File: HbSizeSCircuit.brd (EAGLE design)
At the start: 38.8 x 45.9 mm, 20 parts

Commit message: add left board file
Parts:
- moved R1 88.1 mm to (-47.0, 44.5), turned to 0 degrees
- moved 100KΩ 87.6 mm to (-48.3, 49.5), flipped to the top, turned to 0 degrees
- moved U$12 80.3 mm to (-38.1, 52.1), flipped to the top, turned to 0 degrees
- moved R2 76.8 mm to (-49.5, 31.8)
- moved U$5 72.9 mm to (-35.6, 55.9)
- moved C1 66.5 mm to (-35.6, 44.5), turned to 0 degrees
- moved R3 65.9 mm to (-16.5, 44.5), turned to 0 degrees
- moved C2 65.5 mm to (-41.9, 44.5)
- moved U$2 64.0 mm to (-41.9, 33.0)
- moved U$8 61.3 mm to (-45.7, 1.27)
- moved U$11 60.9 mm to (-27.9, 52.1), flipped to the top
- moved R5 58.3 mm to (-29.2, 44.5), turned to 0 degrees
- moved U$4 58.1 mm to (-29.2, 55.9)
- moved U$9 50.4 mm to (-17.8, 52.1), flipped to the top
- moved U$6 50.3 mm to (-22.9, 14.0), flipped to the top, turned to 0 degrees
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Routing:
- net GND: track 142.9 -> 0.00 mm, vias 5 -> 0
- net +5V: track 72.8 -> 0.00 mm, vias 4 -> 0
- net V+: track 48.4 -> 0.00 mm
- net PIN_THUMBSERVO: track 38.0 -> 0.00 mm
- net SWITCH_INIT: track 36.3 -> 0.00 mm, vias 1 -> 0
- net PIN_ON/OFF: track 32.0 -> 0.00 mm, vias 1 -> 0
- net SWITCH_THUMB: track 30.8 -> 0.00 mm, vias 1 -> 0
- net PIN_INDEXSERVO: track 30.0 -> 0.00 mm
- net PGOOD: track 30.0 -> 0.00 mm, vias 1 -> 0
- net PIN_OTHERSERVO: track 26.4 -> 0.00 mm, vias 2 -> 0
- net SENSOR: track 25.3 -> 0.00 mm, vias 1 -> 0
- net SWITCH_MODE: track 23.8 -> 0.00 mm, vias 1 -> 0
- net SWITCH_HOLD: track 9.90 -> 0.00 mm, vias 1 -> 0
- net N$1: track 3.46 -> 0.00 mm
- net N$2: track 2.66 -> 0.00 mm
- removed copper zone on layer 1, net GND
- removed copper zone on layer 16, net GND
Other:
- board size 38.8 x 45.9 mm -> 6.1 x 10.3 mm

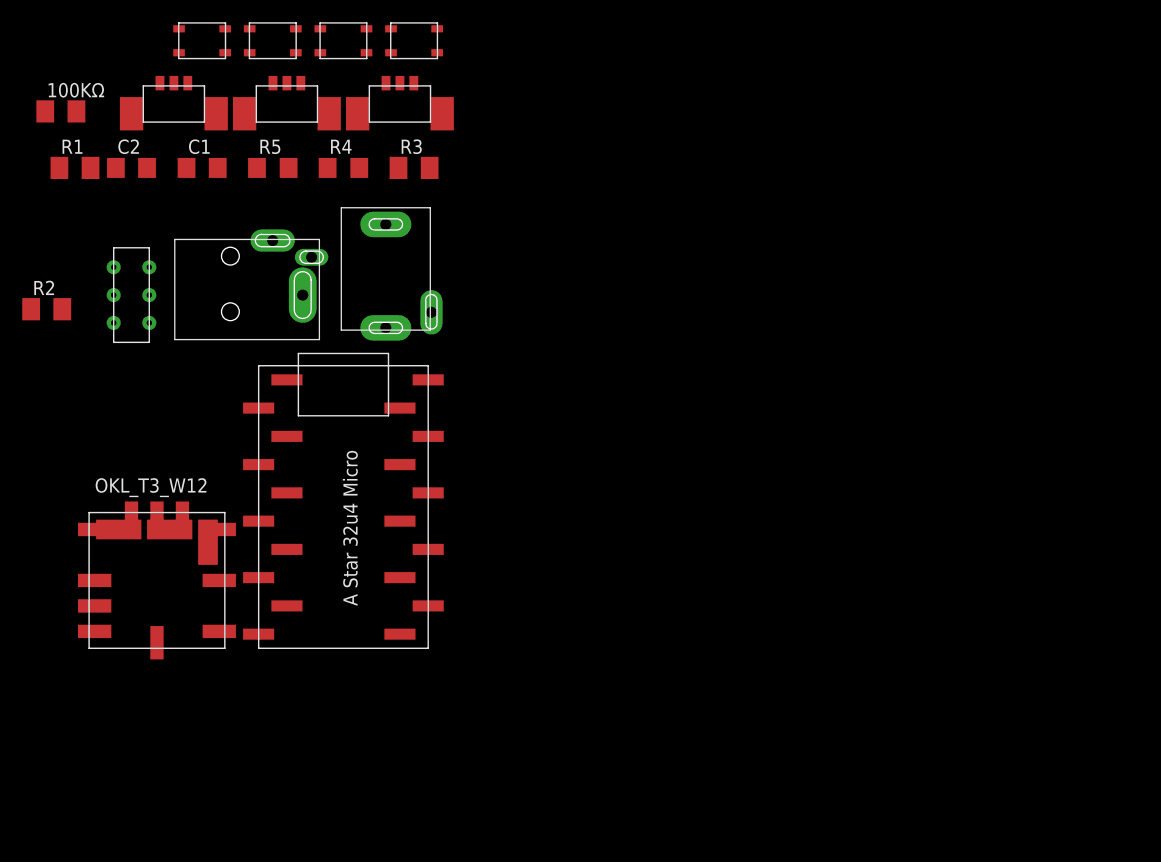
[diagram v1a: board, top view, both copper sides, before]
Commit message: add board layout
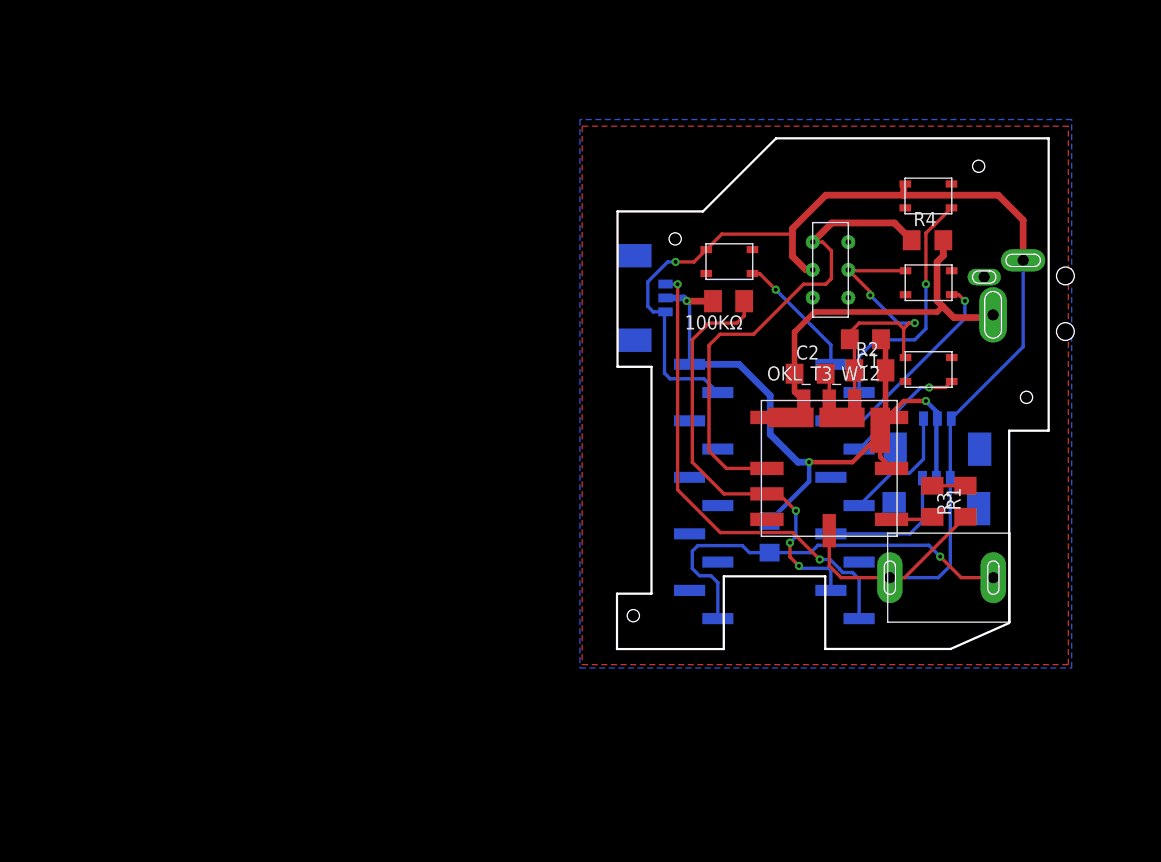
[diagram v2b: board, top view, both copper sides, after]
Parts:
- U$10: value MJ147D -> MJ147D_2PIN; device HbHandBoard_SizeS:MJ147D -> HbHandBoard_SizeS:MJ147D_2PIN
- moved R1 82.7 mm to (30.1, 14.5), turned to 270 degrees
- moved U$7 75.1 mm to (42.0, 31.2), flipped to the bottom
- moved R2 74.2 mm to (24.5, 26.2)
- moved U$11 68.3 mm to (30.4, 16.6), flipped to the bottom
- moved U$4 65.9 mm to (29.7, 26.3)
- moved C2 63.7 mm to (19.1, 25.9)
- moved U$10 63.2 mm to (35.6, 7.62), turned to 270 degrees
- moved U$2 62.9 mm to (20.9, 35.3)
- moved 100KΩ 62.4 mm to (11.8, 32.5), turned to 180 degrees
- moved C1 61.6 mm to (24.1, 29.1), turned to 180 degrees
- moved U$8 61.3 mm to (14.7, 11.3)
- moved R3 57.9 mm to (33.0, 14.5), turned to 90 degrees
- moved U$9 56.9 mm to (30.5, 21.9), flipped to the bottom
- moved U$3 56.9 mm to (29.7, 34.1)
- moved R5 55.6 mm to (15.4, 11.3), flipped to the bottom, turned to 90 degrees
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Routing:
- net GND: track 0.00 -> 152.0 mm, vias 0 -> 3
- net +5V: track 0.00 -> 65.4 mm, vias 0 -> 3
- net PIN_ON/OFF: track 0.00 -> 43.6 mm
- net PIN_INDEXSERVO: track 0.00 -> 42.8 mm, vias 0 -> 2
- net PGOOD: track 0.00 -> 39.3 mm, vias 0 -> 3
- net SENSOR: track 0.00 -> 36.6 mm, vias 0 -> 1
- net V+: track 0.00 -> 36.4 mm
- net SWITCH_INIT: track 0.00 -> 22.1 mm, vias 0 -> 1
- net SWITCH_MODE: track 0.00 -> 18.9 mm, vias 0 -> 1
- net PIN_OTHERSERVO: track 0.00 -> 12.6 mm
- net SWITCH_HOLD: track 0.00 -> 11.5 mm, vias 0 -> 1
- net PIN_THUMBSERVO: track 0.00 -> 11.2 mm
- net SWITCH_THUMB: track 0.00 -> 10.8 mm, vias 0 -> 1
- net N$1: track 0.00 -> 3.76 mm
- net N$2: track 0.00 -> 2.97 mm
- added copper zone on layer 1, net GND
- added copper zone on layer 16, net GND
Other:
- board size 6.1 x 10.3 mm -> 38.8 x 45.9 mm
